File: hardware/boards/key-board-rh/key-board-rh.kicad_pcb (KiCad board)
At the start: 2 copper layers, 153 x 42 mm, 37 parts, among them J1 12-way, J2 2x12 1.27mm shrouded box head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, J3 1x10 2.54mm header pins, J4 1x10 2.54mm header pins, J5 4 wire pads, SW1 KS-33, SW2 KS-33, SW3 KS-33, SW4 KS-33, SW5 KS-33, SW6 KS-33, U1 74HCS165

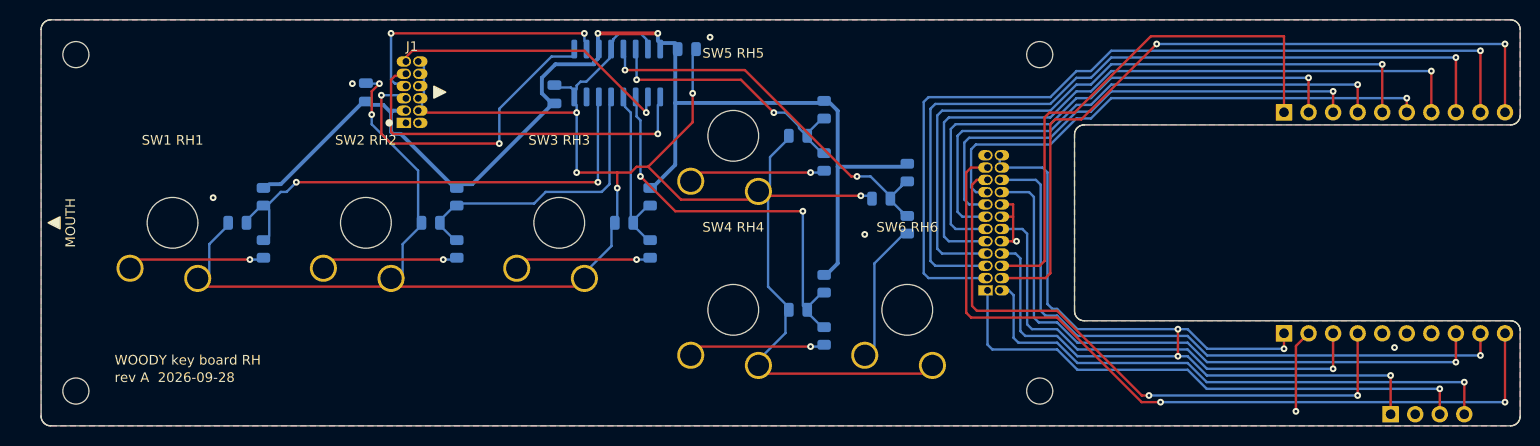
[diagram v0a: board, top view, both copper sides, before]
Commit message: WIP #23: Matrix carrier (option c) in progress - RH key board back to its original outline, EN/IO0 removed, HDR-SERVICE 1x3, carrier sheet and CAD, J-MCU at y 14.9
Checkpoint committed by the coordinator to protect uncommitted work.

Gate-Red: carrier and RH board mid-layout, CAD outputs and sims not rebuilt

Co-Authored-By: Claude Opus 5.5 <noreply@anthropic.com>
Claude-Session: https://claude.ai/code/session_01LmB4muFXnoLprWX4JzuJ5A
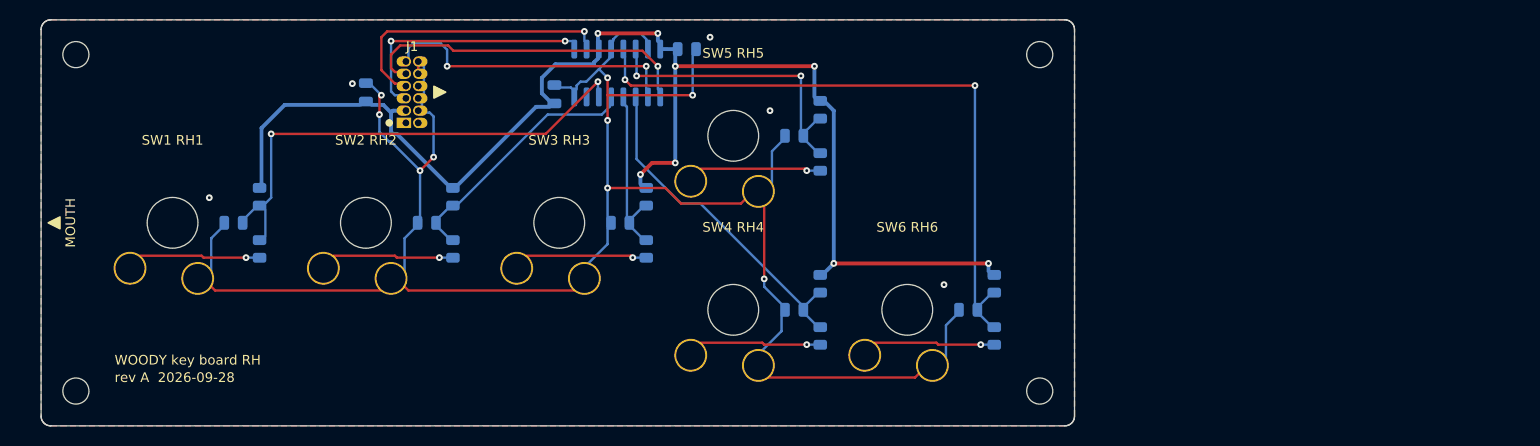
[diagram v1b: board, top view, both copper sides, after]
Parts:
- removed J2: 2x12 1.27mm shrouded box header, woody:IDC-Header_2x12_P1.27mm_XKB_X1270WR_Horizontal
- removed J3, J4: 1x10 2.54mm header pins, Connector_PinHeader_2.54mm:PinHeader_1x10_P2.54mm_Vertical
- removed J5: 4 wire pads, Connector_PinHeader_2.54mm:PinHeader_1x04_P2.54mm_Vertical
- moved C6 14.6 mm to (300.3, 130.5)
- moved R12 14.6 mm to (303.0, 127.8)
- moved R11 14.6 mm to (303.0, 133.2)
- moved R1 0.40 mm to (227.0, 124.2)
- moved R2 0.40 mm to (227.0, 118.8)
- moved R3 0.40 mm to (247.0, 124.2)
- moved R4 0.40 mm to (247.0, 118.8)
- moved C1 0.40 mm to (224.3, 121.5)
- moved C2 0.40 mm to (244.3, 121.5)
- moved C3 0.40 mm to (264.3, 121.5)
- moved C4 0.40 mm to (282.3, 130.5)
- moved C5 0.40 mm to (282.3, 112.5)
- moved R10 0.40 mm to (285.0, 109.8)
- moved R7 0.40 mm to (285.0, 133.2)
- moved R8 0.40 mm to (285.0, 127.8)
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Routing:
- net /INST_5V_A: track 104.9 -> 0.00 mm, vias 4 -> 0
- net /U0TXD: track 90.7 -> 0.00 mm, vias 1 -> 0
- net /IO40: track 84.1 -> 0.00 mm, vias 1 -> 0
- net /IO1: track 83.6 -> 0.00 mm, vias 2 -> 0
- net /U0RXD: track 78.4 -> 0.00 mm, vias 2 -> 0
- net /IO39: track 73.4 -> 0.00 mm, vias 1 -> 0
- net /IO37: track 72.4 -> 0.00 mm, vias 1 -> 0
- net /IO2: track 67.2 -> 0.00 mm, vias 1 -> 0
- net /IO3: track 64.8 -> 0.00 mm, vias 1 -> 0
- net /IO7: track 64.5 -> 0.00 mm, vias 2 -> 0
- net /IO0: track 57.9 -> 0.00 mm, vias 1 -> 0
- net /IO36: track 57.6 -> 0.00 mm, vias 1 -> 0
- net /EN: track 56.9 -> 0.00 mm, vias 1 -> 0
- net /IO34: track 56.6 -> 0.00 mm, vias 1 -> 0
- net /IO33: track 55.8 -> 0.00 mm
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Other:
- board size 153 x 42 mm -> 106.9 x 42 mm
- board text removed: "J2"
- board text removed: "J3"
- board text removed: "J4"
- board text removed: "J5"

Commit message: #6 #17 #19: checkpoint - RH heights, per-board kicad check, Standard PCBA, THT trim, rev A
#19 F2: key-board-rh layout.yaml heights: table (same parts as LH).
#6-3: tools/kicad.py check --board <name>; the three order sheets gate on it.
#6-6: preview checklist item for JLC's rails and tooling holes.
#17 D1/D6: owner chose Standard PCBA (ADR 0028 amendment 2026-10-04); order
sheets updated, D6 moot.
#8-11: owner chose trim length (ADR 0017 amendment 2026-10-04); layout.yaml
hand_trim: and pcb.py render's Fit column on the hand-assembly list.
#6-7: every board rev A on first fabrication (ADR 0020 Amendment 9); key boards'
silk and title blocks set and re-rendered.

Gate-Red: check-staleness cad - photo renders stale against the key boards' silk change, cad.py build in progress (checkpoint); sim - boards/module-iso has no tooling.md coverage row (pre-existing); kicad.py check - module-main.kicad_pcb DRC/route errors and stale module-main renders (pre-existing, another board under work)

Co-Authored-By: Claude Opus 5.5 <noreply@anthropic.com>
Claude-Session: https://claude.ai/code/session_01LmB4muFXnoLprWX4JzuJ5A
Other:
- board text added: "rev A 2026-10-03"
- board text removed: "rev A 2026-09-28"
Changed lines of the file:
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@@
 	(title_block
 		(title "WOODY key board RH")
-		(date "2026-09-28")
+		(date "2026-10-03")
 		(rev "A")
 	)
@@
 		)
 	)
-	(gr_text "rev A  2026-09-28"
+	(gr_text "rev A  2026-10-03"
 		(at 212 137.5 0)
 		(layer "F.SilkS")
@@
 		)
 	)
-	(gr_text "rev A  2026-09-28"
+	(gr_text "rev A  2026-10-03"
 		(at 212 139.3 0)
 		(layer "B.SilkS")

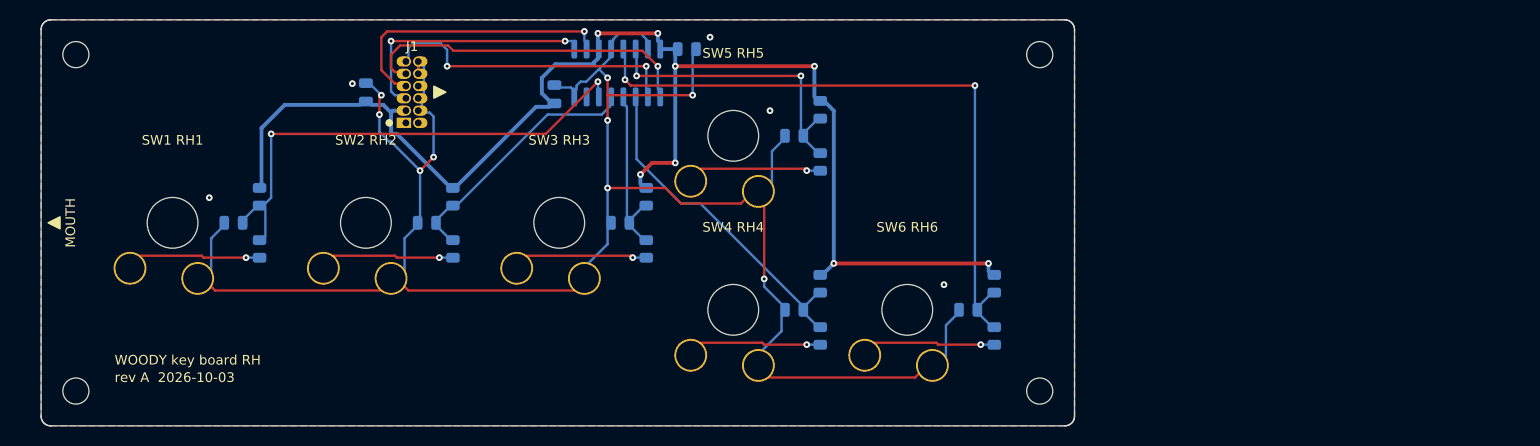
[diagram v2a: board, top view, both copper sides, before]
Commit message: #43: key-board-rh - mouth end lengthened to the body CAD's outline, H1/H2 and their keep-outs moved with it
As key-board-lh: the mouth edge, the two mouth mounts, their keep-outs and
the pours' mouth edge moved 2.2 mm toward the mouth, to
mechanical/export/key-board-rh.dxf and pcb-geometry.echo. Every part and
track where it was; pours refilled. pcb.py check: 0 errors;
kicad.py check --board key-board-rh: PASS; renders and fab/ rebuilt.

Gate-Red: tools/cad.py check - 43 body renders, photos and the clash stale, left for the final render pass as directed; kicad: main-board still disagrees with the CAD (its mount moves are held for the routing trial, as directed).
Co-Authored-By: Claude Opus 5.5 <noreply@anthropic.com>
Claude-Session: https://claude.ai/code/session_01LmB4muFXnoLprWX4JzuJ5A
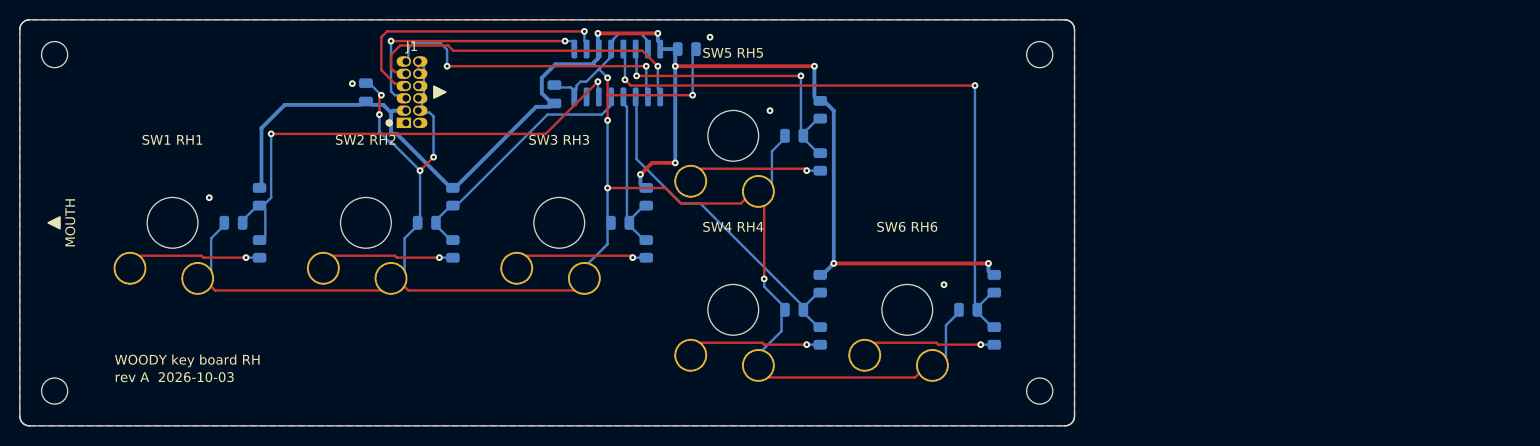
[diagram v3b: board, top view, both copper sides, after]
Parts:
- moved H1 2.20 mm to (205.8, 138.9)
- moved H2 2.20 mm to (205.8, 104.1)
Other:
- board size 106.9 x 42 mm -> 109.1 x 42 mm
